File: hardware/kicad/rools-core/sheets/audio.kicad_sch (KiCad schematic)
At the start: 0 parts

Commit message: Add QSPI settings persistence, CV calibration app, and CV output driver.
Co-authored-by: Cursor <cursoragent@cursor.com>
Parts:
- added C21, C23, C27, C28, C29, C30: 47pF, symbol Device:C
- added C22, C24: 560pF, symbol Device:C
- added C25, C26, C31, C32: 100nF, symbol Device:C
- added J_CV_5, J_CV_6, J_CV_7, J_CV_8: (no value), ES_Daisy_Patch_Rev8:PJ301M-12SLOT, symbol patch-eagle:EURO_JACK_PJ301M-12
- added R44, R45, R46, R49, R50, R51, R56, R57, R58, R59, R60, R61: 100k, symbol Device:R
- added R47, R52: 10k, symbol Device:R
- added R48, R53, R62, R63: 1K, symbol Device:R
- added R54, R55: 10K, symbol Device:R
- added U7, U8: TL074, symbol Amplifier_Operational:TL074
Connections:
- net +12V: now also C25.2, C31.2, U7.4 (V+), U8.4 (V+)
- net -12V: now also C26.1, C32.1, U7.11 (V-), U8.11 (V-)
- net GND: now also C25.1, C26.2, C31.1, C32.2, J_CV_5.GND, J_CV_5.GND2 (GND), J_CV_5.SW (NORM), J_CV_5.SW2 (NORM), J_CV_6.GND, J_CV_6.GND2 (GND), J_CV_6.SW (NORM), J_CV_6.SW2 (NORM), J_CV_7.GND, J_CV_7.GND2 (GND), J_CV_7.SW (NORM), J_CV_7.SW2 (NORM), J_CV_8.GND, J_CV_8.GND2 (GND), J_CV_8.SW (NORM), J_CV_8.SW2 (NORM), U7.10 (+), U7.12 (+), U7.3 (+), U7.5 (+), U8.10 (+), U8.12 (+), U8.3 (+), U8.5 (+)
- new net: C28.1, R55.2, R57.1, U8.6 (-)
- new net: C28.2, R57.2, R59.1, U8.7
- new net: C27.2, R56.2, R58.1, U8.1
- new net: C27.1, R54.2, R56.1, U8.2 (-)
- new net: C29.1, R58.2, R60.1, U8.13 (-)
- new net: C30.2, R61.2, R63.1, U8.8
- new net: C30.1, R59.2, R61.1, U8.9 (-)
- new net: J_CV_6.TIP, J_CV_6.TIP2 (TIP), R49.1
- new net: C21.1, R44.2, R45.1, U7.2 (-)
- new net: C21.2, R45.2, R46.1, U7.1
- new net: C23.2, R50.2, R51.1, U7.7
- new net: C24.1, R51.2, R52.1, U7.9 (-)
- new net: C23.1, R49.2, R50.1, U7.6 (-)
- new net: C22.1, R46.2, R47.1, U7.13 (-)
- new net: C29.2, R60.2, R62.1, U8.14
- new net: J_CV_7.TIP, J_CV_7.TIP2 (TIP), R62.2
- new net: C22.2, R47.2, R48.1, U7.14
- new net: C24.2, R52.2, R53.1, U7.8
- new net: J_CV_5.TIP, J_CV_5.TIP2 (TIP), R44.1
- new net: J_CV_8.TIP, J_CV_8.TIP2 (TIP), R63.2
- new net AUDIO_IN_L: R48.2
- new net AUDIO_IN_R: R53.2
- new net AUDIO_OUT_L: R54.1
- new net AUDIO_OUT_R: R55.1

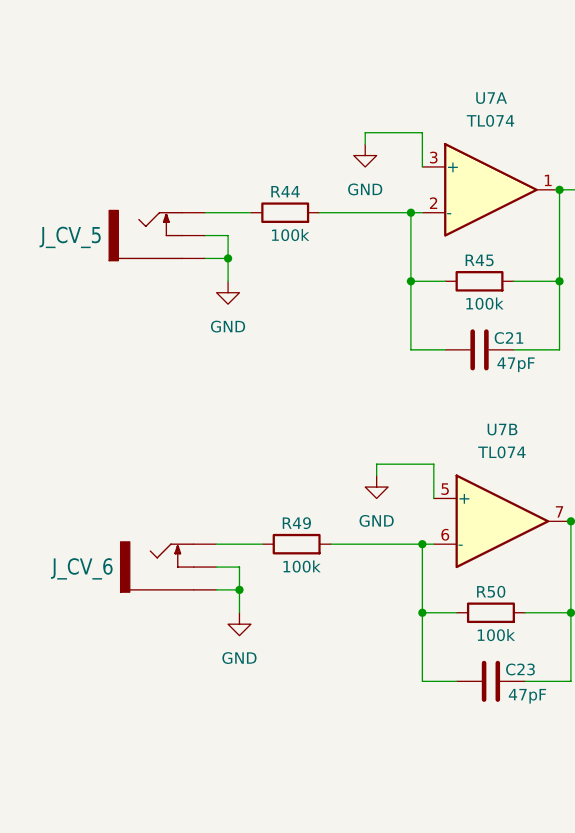
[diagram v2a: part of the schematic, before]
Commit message: Align Core with onboard audio and split CV/Knob ADC architecture.
Document Seed pin16–19 + TL074 (no PCM3060), 8-way ADC firmware synthesis, Enc/Knob pin remap, EXTI_PWR on D28, and update KiCad seed/CV/audio sheets accordingly.

Co-authored-by: Cursor <cursoragent@cursor.com>
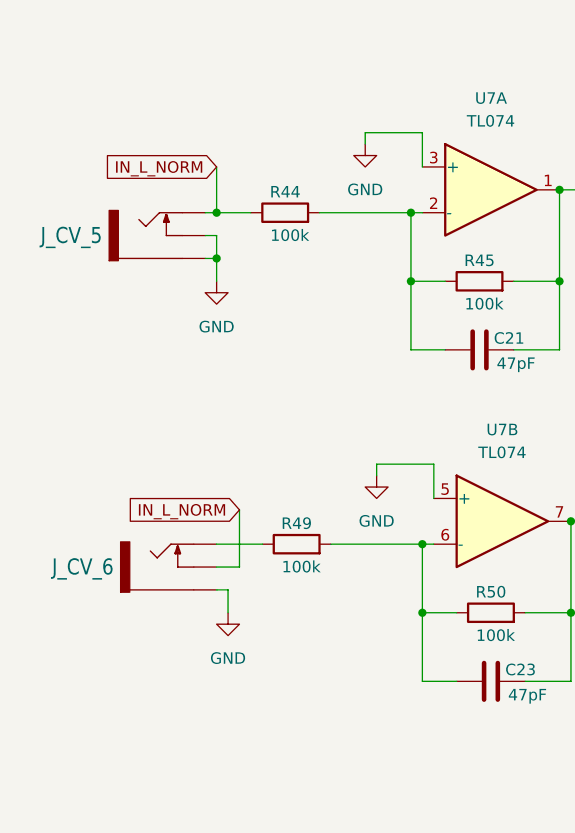
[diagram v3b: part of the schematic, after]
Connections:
- net GND: no longer J_CV_6.SW (NORM), J_CV_6.SW2 (NORM)
- net IN_L_NORM: now reaches J_CV_5.TIP, J_CV_5.TIP2 (TIP), R44.1
- net IN_L_NORM: now also J_CV_6.SW (NORM), J_CV_6.SW2 (NORM)
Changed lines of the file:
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@@
 	)
 	(junction
+		(at 36.83 59.69)
+		(diameter 0)
+		(color 0 0 0 0)
+	)
+	(junction
 		(at 227.33 88.9)
 		(diameter 0)
@@
 	)
 	(junction
-		(at 39.37 101.6)
-		(diameter 0)
-		(color 0 0 0 0)
-	)
-	(junction
 		(at 116.84 101.6)
 		(diameter 0)
@@
 	)
 	(junction
-		(at 38.1 64.77)
+		(at 186.69 99.06)
 		(diameter 0)
 		(color 0 0 0 0)
 	)
 	(junction
-		(at 186.69 99.06)
+		(at 243.84 86.36)
 		(diameter 0)
 		(color 0 0 0 0)
 	)
 	(junction
-		(at 243.84 86.36)
+		(at 245.11 59.69)
 		(diameter 0)
 		(color 0 0 0 0)
 	)
 	(junction
-		(at 245.11 59.69)
+		(at 36.83 64.77)
 		(diameter 0)
 		(color 0 0 0 0)
@@
 	(wire
 		(pts
-			(xy 38.1 62.23) (xy 38.1 64.77)
-		)
-		(stroke
-			(width 0)
-			(type default)
-		)
-	)
-	(wire
-		(pts
 			(xy 259.08 54.61) (xy 261.62 54.61)
 		)
@@
 	(wire
 		(pts
-			(xy 38.1 64.77) (xy 35.56 64.77)
+			(xy 35.56 64.77) (xy 36.83 64.77)
 		)
 		(stroke
@@
 	(wire
 		(pts
-			(xy 40.64 59.69) (xy 35.56 59.69)
-		)
-		(stroke
-			(width 0)
-			(type default)
-		)
-	)
-	(wire
-		(pts
 			(xy 99.06 64.77) (xy 99.06 72.39)
 		)
@@
 	(wire
 		(pts
-			(xy 38.1 64.77) (xy 38.1 67.31)
+			(xy 36.83 64.77) (xy 36.83 67.31)
 		)
 		(stroke
@@
 	(wire
 		(pts
+			(xy 39.37 92.71) (xy 39.37 99.06)
+		)
+		(stroke
+			(width 0)
+			(type default)
+		)
+	)
+	(wire
+		(pts
 			(xy 238.76 96.52) (xy 243.84 96.52)
 		)
@@
 	(wire
 		(pts
-			(xy 39.37 101.6) (xy 39.37 104.14)
+			(xy 38.1 101.6) (xy 38.1 104.14)
+		)
+		(stroke
+			(width 0)
+			(type default)
+		)
+	)
+	(wire
+		(pts
+			(xy 35.56 59.69) (xy 36.83 59.69)
 		)
 		(stroke
@@
 	(wire
 		(pts
+			(xy 36.83 62.23) (xy 36.83 64.77)
+		)
+		(stroke
+			(width 0)
+			(type default)
+		)
+	)
+	(wire
+		(pts
 			(xy 102.87 72.39) (xy 99.06 72.39)
 		)
@@
 	(wire
 		(pts
+			(xy 36.83 59.69) (xy 40.64 59.69)
+		)
+		(stroke
+			(width 0)
+			(type default)
+		)
+	)
+	(wire
+		(pts
 			(xy 220.98 78.74) (xy 220.98 80.01)
 		)
@@
 	(wire
 		(pts
+			(xy 36.83 54.61) (xy 36.83 59.69)
+		)
+		(stroke
+			(width 0)
+			(type default)
+		)
+	)
+	(wire
+		(pts
 			(xy 245.11 59.69) (xy 245.11 49.53)
 		)
@@
 	(wire
 		(pts
-			(xy 38.1 62.23) (xy 35.56 62.23)
+			(xy 36.83 62.23) (xy 35.56 62.23)
 		)
 		(stroke
@@
 	(wire
 		(pts
-			(xy 39.37 99.06) (xy 39.37 101.6)
-		)
-		(stroke
-			(width 0)
-			(type default)
-		)
-	)
-	(wire
-		(pts
 			(xy 111.76 109.22) (xy 116.84 109.22)
 		)
@@
 	(wire
 		(pts
-			(xy 204.47 69.85) (xy 204.47 62.23)
+			(xy 39.37 99.06) (xy 36.83 99.06)
 		)
 		(stroke
@@
 	(wire
 		(pts
-			(xy 39.37 99.06) (xy 36.83 99.06)
+			(xy 204.47 69.85) (xy 204.47 62.23)
 		)
 		(stroke
@@
 	(wire
 		(pts
-			(xy 39.37 101.6) (xy 36.83 101.6)
+			(xy 38.1 101.6) (xy 36.83 101.6)
 		)
 		(stroke
@@
 		)
 	)
+	(global_label "IN_L_NORM"
+		(shape input)
+		(at 36.83 54.61 180)
+		(fields_autoplaced yes)
+		(effects
+			(font
+				(size 1.27 1.27)
+			)
+			(justify right)
+		)
+		(property "Intersheetrefs" "${INTERSHEET_REFS}"
+			(at 23.4687 54.61 0)
+			(hide yes)
+			(show_name no)
+			(do_not_autoplace no)
+			(effects
+				(font
+					(size 1.27 1.27)
+				)
+				(justify right)
+			)
+		)
+	)
 	(global_label "AUDIO_IN_L"
 		(shape output)
@@
 		)
 	)
+	(global_label "IN_L_NORM"
+		(shape input)
+		(at 39.37 92.71 180)
+		(fields_autoplaced yes)
+		(effects
+			(font
+				(size 1.27 1.27)
+			)
+			(justify right)
+		)
+		(property "Intersheetrefs" "${INTERSHEET_REFS}"
+			(at 26.0087 92.71 0)
+			(hide yes)
+			(show_name no)
+			(do_not_autoplace no)
+			(effects
+				(font
+					(size 1.27 1.27)
+				)
+				(justify right)
+			)
+		)
+	)
 	(global_label "AUDIO_OUT_L"
 		(shape input)
@@
 	(symbol
 		(lib_id "power:GND")
-		(at 39.37 104.14 0)
+		(at 38.1 104.14 0)
 		(unit 1)
 		(body_style 1)
@@
 		(fields_autoplaced yes)
 		(property "Reference" "#PWR048"
-			(at 39.37 110.49 0)
+			(at 38.1 110.49 0)
 			(hide yes)
 			(show_name no)
@@
 		)
 		(property "Value" "GND"
-			(at 39.37 109.22 0)
+			(at 38.1 109.22 0)
 			(show_name no)
 			(do_not_autoplace no)
@@
 		)
 		(property "Footprint" ""
-			(at 39.37 104.14 0)
+			(at 38.1 104.14 0)
 			(hide yes)
 			(show_name no)
@@
 		)
 		(property "Datasheet" ""
-			(at 39.37 104.14 0)
+			(at 38.1 104.14 0)
 			(hide yes)
 			(show_name no)
@@
 		)
 		(property "Description" "Power symbol creates a global label with name \"GND\" , ground"
-			(at 39.37 104.14 0)
+			(at 38.1 104.14 0)
 			(hide yes)
 			(show_name no)
@@
 	(symbol
 		(lib_id "power:GND")
-		(at 38.1 67.31 0)
+		(at 36.83 67.31 0)
 		(unit 1)
 		(body_style 1)
@@
 		(fields_autoplaced yes)
 		(property "Reference" "#PWR041"
-			(at 38.1 73.66 0)
+			(at 36.83 73.66 0)
 			(hide yes)
 			(show_name no)
@@
 		)
 		(property "Value" "GND"
-			(at 38.1 72.39 0)
+			(at 36.83 72.39 0)
 			(show_name no)
 			(do_not_autoplace no)
@@
 		)
 		(property "Footprint" ""
-			(at 38.1 67.31 0)
+			(at 36.83 67.31 0)
 			(hide yes)
 			(show_name no)
@@
 		)
 		(property "Datasheet" ""
-			(at 38.1 67.31 0)
+			(at 36.83 67.31 0)
 			(hide yes)
 			(show_name no)
@@
 		)
 		(property "Description" "Power symbol creates a global label with name \"GND\" , ground"
-			(at 38.1 67.31 0)
+			(at 36.83 67.31 0)
 			(hide yes)
 			(show_name no)

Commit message: Finalize Core schematic pin map and JLC BOM for assembly.
MIDI USART1 on D13/D14, DAC8565 on D26/D27, and document P2 EXP_BUS so Exp I/O no longer conflicts with CV Out.

Co-authored-by: Cursor <cursoragent@cursor.com>
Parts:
- C21, C23, C27, C28, C29, C30: footprint (none) -> Capacitor_SMD:C_0603_1608Metric; LCSC (none) -> C1653
- C22, C24: footprint (none) -> Capacitor_SMD:C_0603_1608Metric; LCSC (none) -> C1680
- C25, C26, C31, C32: footprint (none) -> Capacitor_SMD:C_0603_1608Metric; LCSC (none) -> C14663
- J_CV_5, J_CV_6, J_CV_7, J_CV_8: footprint ES_Daisy_Patch_Rev8:PJ301M-12SLOT -> Connector_Audio:Jack_3.5mm_QingPu_WQP-PJ398SM_Vertical_CircularHoles
- R44, R45, R46, R49, R50, R51, R56, R57, R58, R59, R60, R61: value 100k -> 100K; footprint (none) -> Resistor_SMD:R_0603_1608Metric; LCSC (none) -> C25803
- R47, R52: value 10k -> 10K; footprint (none) -> Resistor_SMD:R_0603_1608Metric; LCSC (none) -> C25804
- R48, R53, R62, R63: footprint (none) -> Resistor_SMD:R_0603_1608Metric; LCSC (none) -> C21190
- R54, R55: footprint (none) -> Resistor_SMD:R_0603_1608Metric; LCSC (none) -> C25804
- U7, U8: footprint (none) -> Package_SO:SOIC-14_3.9x8.7mm_P1.27mm; LCSC (none) -> C6964

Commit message: Lay out Core front-panel PCB for 10HP Eurorack fit.
Use RK09L 3-pin no-MP pots, split Daisy daughterboard, audio jack refs, and local display footprint library.

Co-authored-by: Cursor <cursoragent@cursor.com>
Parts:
- removed J_CV_5, J_CV_6, J_CV_7, J_CV_8: (no value), Connector_Audio:Jack_3.5mm_QingPu_WQP-PJ398SM_Vertical_CircularHoles, symbol patch-eagle:EURO_JACK_PJ301M-12
- added J_AI_L1, J_AI_R1, J_AO_L1, J_AO_R1: AudioJack2_SwitchT, Connector_Audio:Jack_3.5mm_QingPu_WQP-PJ398SM_Vertical_CircularHoles, symbol Connector_Audio:AudioJack2_SwitchT
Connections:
- net GND: now also J_AI_L1.T, J_AI_L1.TN, J_AI_R1.TN, J_AO_L1.T, J_AO_L1.TN, J_AO_R1.T, J_AO_R1.TN
- net IN_L_NORM: now also J_AI_L1.S, J_AI_R1.T
- net at R49.1: now also J_AI_R1.S
- net at R62.2: now also J_AO_L1.S
- net at R63.2: now also J_AO_R1.S

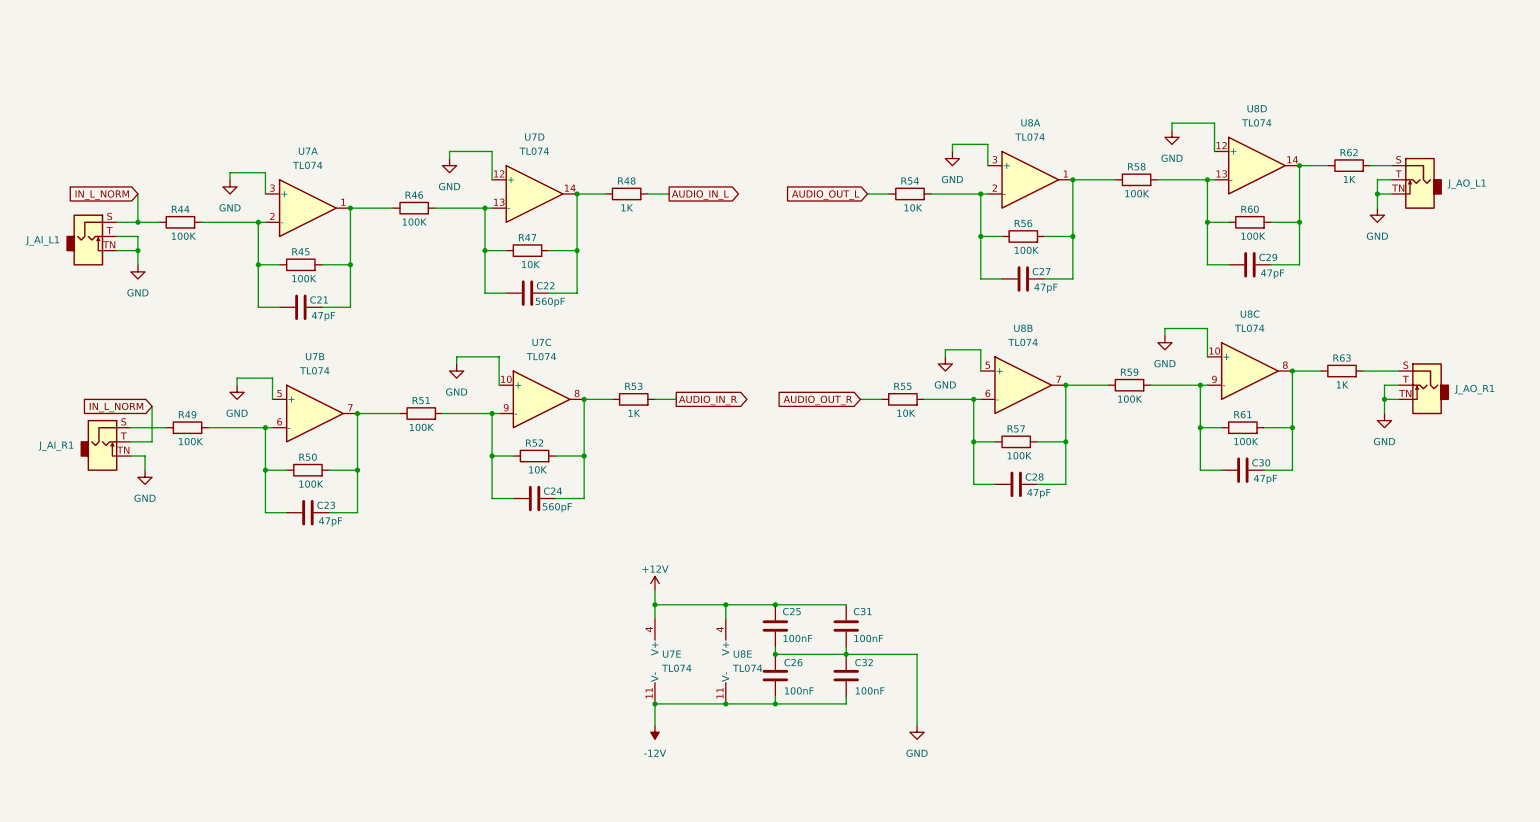
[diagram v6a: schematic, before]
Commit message: Route Core PCB and place Daisy Seed on the daughterboard.
Sync schematic sheets with the split-board layout and updated interconnects.

Co-authored-by: Cursor <cursoragent@cursor.com>
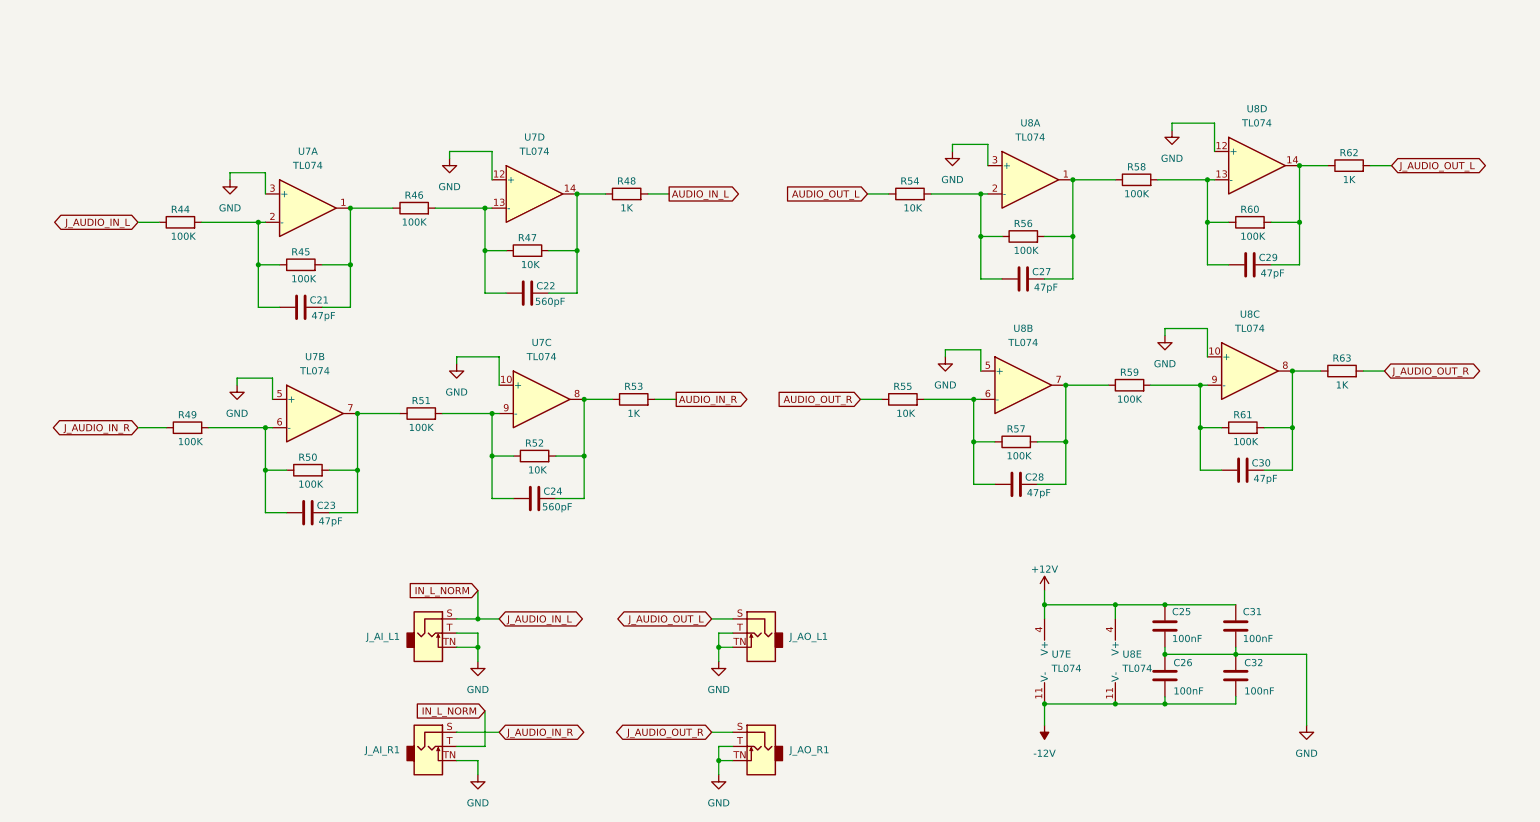
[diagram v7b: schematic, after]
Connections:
- net J_AUDIO_IN_R: now reaches J_AI_R1.S, R49.1
- net J_AUDIO_OUT_L: now reaches J_AO_L1.S, R62.2
- net J_AUDIO_OUT_R: now reaches J_AO_R1.S, R63.2
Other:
- moved on the sheet: C25, C26, C31, C32, J_AI_L1, J_AI_R1, J_AO_L1, J_AO_R1, U7E, U8E
